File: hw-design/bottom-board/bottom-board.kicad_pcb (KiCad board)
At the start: 2 copper layers, 172 x 140.5 mm, 240 parts, among them J1 RJ45_LEDS, J2 JACK_TRS_6PINS, J3 JACK_TRS_6PINS, J4 JACK_TRS_6PINS, J5 JACK_TRS_6PINS, J6 JACK_TRS_6PINS, K1 IM03, K2 IM03, P1 USB_B, P2 USB_A, P3 DIN_5, P4 DIN_5, P5 BARREL_JACK, P6 CONN_02X10, P7 CONN_01X10, P9 CONN_01X03, Q1 J112, Q10 2N7002, Q11 2N7002, Q12 2N7002, Q13 2N7002, Q14 2N7002, Q15 2N7002, Q2 J112, Q3 2N7002, Q4 2N7002, Q5 J112, Q6 J112, Q7 2N7002, Q8 2N7002, Q9 2N7002, SW1 SW_PUSH, U1 MCP1754ST-5002E/MB, U10 LM4811, U11 RT9701, U12 6N137S, U13 ISL83491, U2 KA7809, U3 NCP1117ST50T3G, U4 NCP1117ST33T3G, U5 CS4245, U6 ICnova_A20_SODIMM, U7 LM4562, U8 LM4562, U9 LM4562

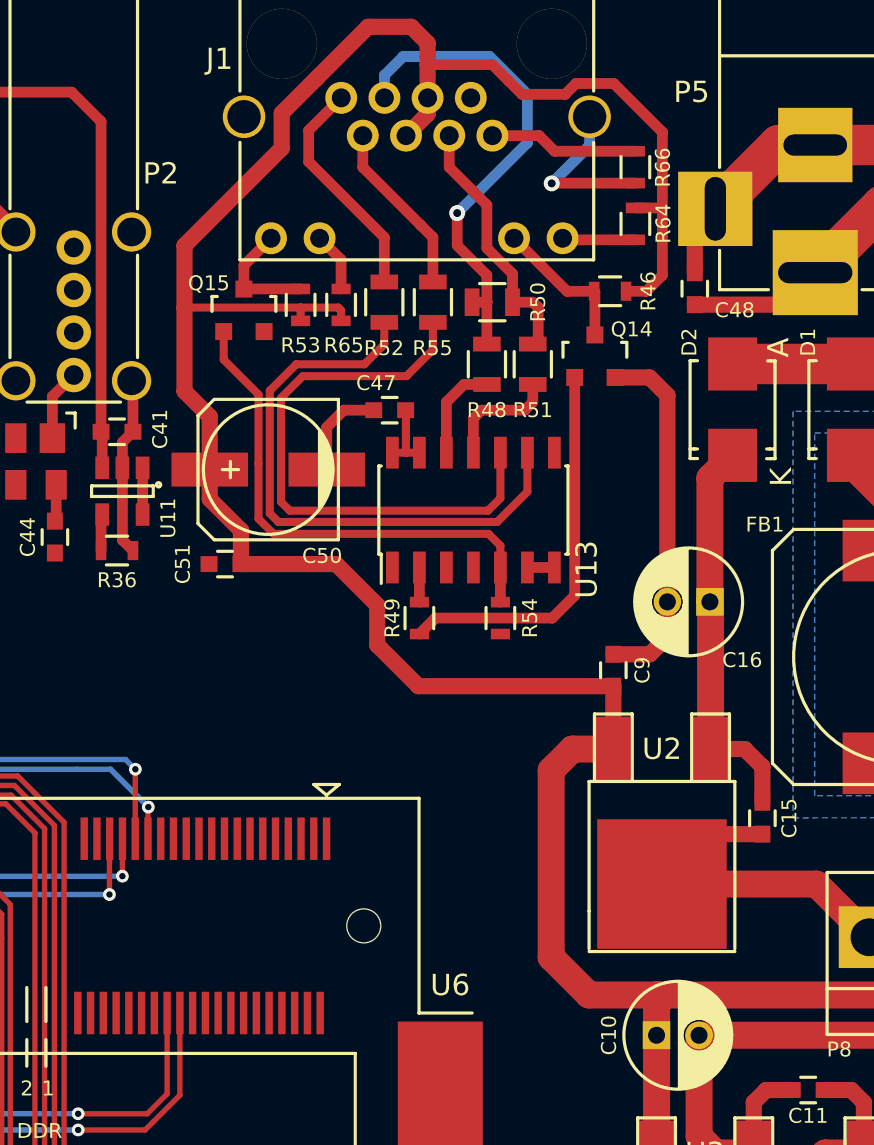
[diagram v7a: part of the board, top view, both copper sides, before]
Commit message: pcb: control chain interface tracks done
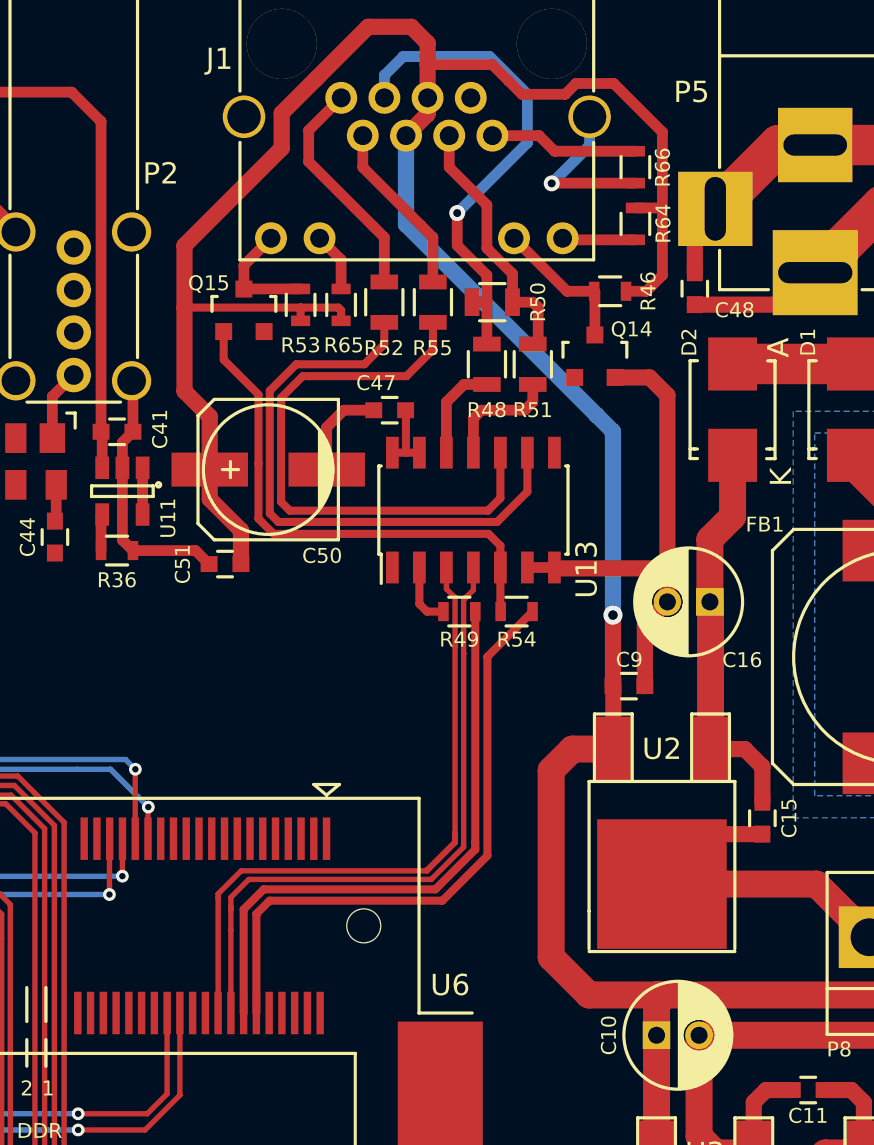
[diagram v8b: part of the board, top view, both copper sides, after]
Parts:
- moved R49 1.90 mm to (189.8, 48.7), turned to 0 degrees
- moved C9 1.05 mm to (197.8, 52.2), turned to 0 degrees
- moved R54 0.82 mm to (192.5, 48.7), turned to 0 degrees
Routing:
- net UART_RE_CHAIN: track 0.03 -> 33.2 mm
- net UART_DE_CHAIN: track 0.00 -> 30.9 mm
- net UART_TX_CHAIN: track 0.00 -> 29.0 mm
- net UART_RX_CHAIN: track 18.3 -> 28.1 mm
- net GNDD: track 205.2 -> 214.2 mm
- net +9V: track 135.8 -> 144.7 mm, vias 0 -> 1
- net Net-(R49-Pad1): track 1.63 -> 3.00 mm
